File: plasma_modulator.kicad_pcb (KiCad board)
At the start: 4 copper layers, 100 x 80 mm, 74 parts, among them P1 CONN_01X03, P2 CONN_01X03, P3 CONN_01X06, P4 CONN_01X04, P5 RCA_1, Q1 MOSFET_N, Q2 MOSFET_N, Q3 MOSFET_N, Q4 MOSFET_N, SW1 SW_PUSH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

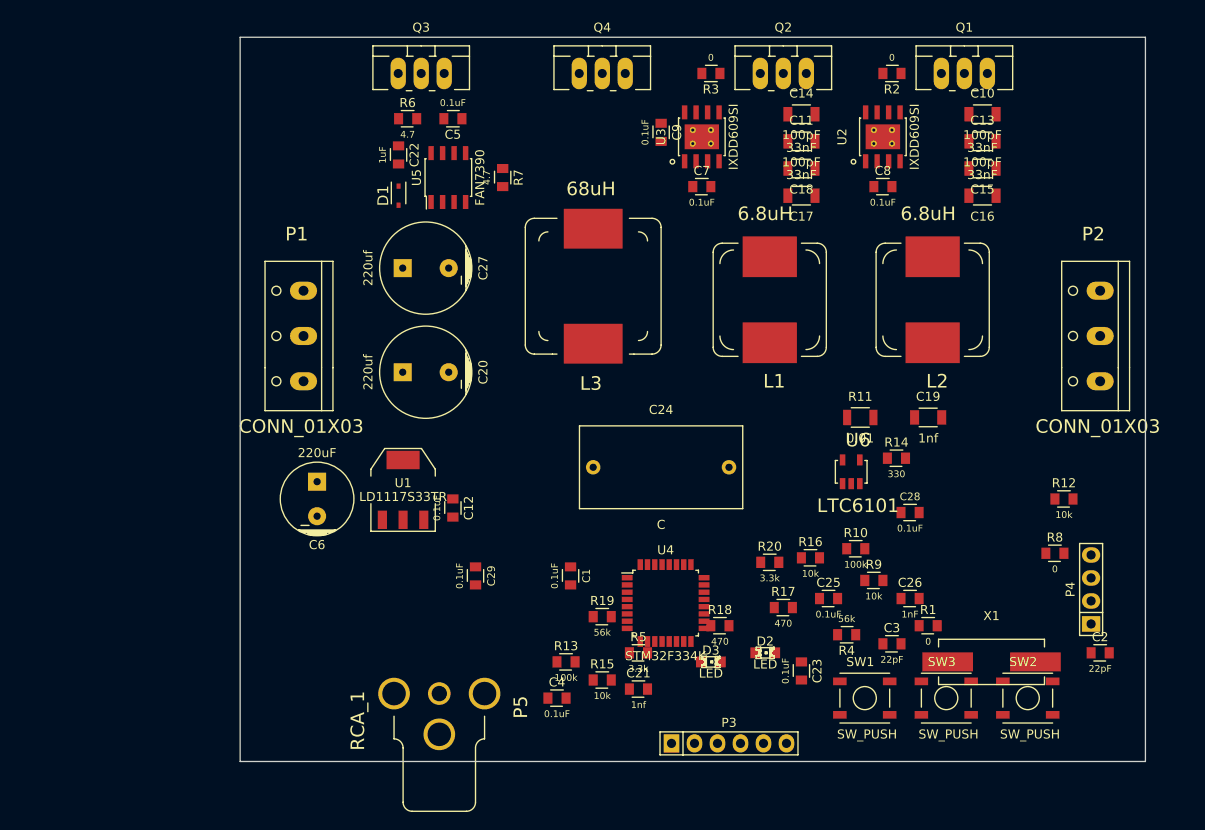
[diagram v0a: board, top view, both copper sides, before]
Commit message: draft of component layout
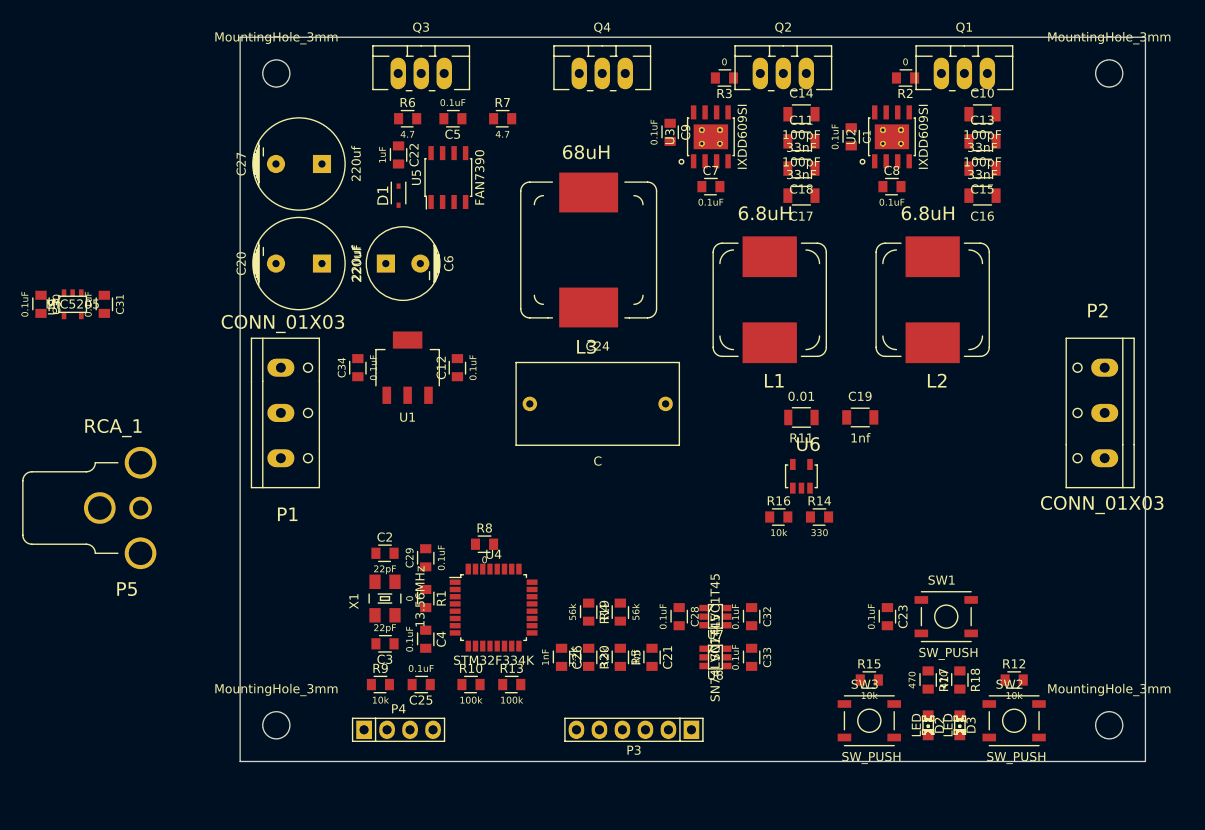
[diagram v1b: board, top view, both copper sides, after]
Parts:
- added C30: 0.1uF, wbraun_library:SMD-0805, F.Cu at (21.0, 80.5)
- added C31: 0.1uF, wbraun_library:SMD-0805, F.Cu at (28.0, 80.5)
- added C32: 0.1uF, wbraun_library:SMD-0805, F.Cu at (99.5, 115.0)
- added C33: 0.1uF, wbraun_library:SMD-0805, F.Cu at (99.5, 119.5)
- added C34: 0.1uF, wbraun_library:SMD-0805, F.Cu at (56.0, 87.5)
- added MountingHole_3mm: VAL**, Mounting_Holes:MountingHole_3mm, F.Cu at (47.0, 55.0)
- added MountingHole_3mm: VAL**, Mounting_Holes:MountingHole_3mm, F.Cu at (139.0, 55.0)
- added MountingHole_3mm: VAL**, Mounting_Holes:MountingHole_3mm, F.Cu at (47.0, 127.0)
- added MountingHole_3mm: VAL**, Mounting_Holes:MountingHole_3mm, F.Cu at (139.0, 127.0)
- added U7: SN74LVC1T45, SMD_Packages:SOT-23-6, F.Cu at (95.5, 115.0)
- added U8: SN74LVC1T45, SMD_Packages:SOT-23-6, F.Cu at (95.5, 119.5)
- added U9: MIC5205, SMD_Packages:SOT-23-5, F.Cu at (24.5, 80.5)
- U1: footprint SMD_Packages:SOT-223 -> wbraun_library:SOT-223
- X1: footprint Crystals:Crystal_HC49-SD_SMD -> wbraun_library:4-SMD
- moved C2 79.8 mm to (59.0, 108.0)
- moved P4 78.1 mm to (60.5, 127.5), turned to 0 degrees
- moved X1 67.4 mm to (59.0, 113.0), turned to 90 degrees
- moved R8 63.0 mm to (70.0, 107.0)
- moved C1 57.6 mm to (110.5, 62.0)
- moved C3 56.0 mm to (59.0, 118.0), turned to 180 degrees
- moved R9 55.7 mm to (58.5, 122.5)
- moved R1 55.6 mm to (63.5, 113.0), turned to 270 degrees
- moved C25 46.0 mm to (63.0, 122.5), turned to 180 degrees
- moved R10 45.1 mm to (68.5, 122.5)
- moved P5 45.1 mm to (27.5, 103.0), turned to 0 degrees
- moved C26 39.0 mm to (78.5, 119.5), turned to 270 degrees
- moved R15 29.5 mm to (112.5, 122.0)
- moved D3 28.4 mm to (122.5, 127.0), turned to 270 degrees
- moved C28 28.0 mm to (91.5, 115.0), turned to 270 degrees
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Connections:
- R17 pad 1: +3.3V -> STATUS_2
- R18 pad 1: STATUS -> STATUS_1
- U4 pad 14: STATUS -> Net-(U4-Pad14)
- U4 pad 20: RF_A -> RF_A_lv
- U4 pad 21: RF_B -> RF_B_lv
- U4 pad 29: Net-(U4-Pad29) -> STATUS_1
- U4 pad 30: Net-(U4-Pad30) -> STATUS_2

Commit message: final component placement
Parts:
- removed R8: 0, wbraun_library:SMD-0805
- moved C30 41.1 mm to (57.5, 99.5)
- moved C31 41.1 mm to (64.5, 99.5)
- moved U9 41.1 mm to (61.0, 99.5)
- moved P5 20.1 mm to (45.5, 112.0)
- moved R16 8.28 mm to (95.0, 100.5), turned to 90 degrees
- moved R11 5.70 mm to (99.5, 94.5)
- moved U6 5.59 mm to (99.5, 100.5)
- moved R14 4.61 mm to (104.0, 100.5), turned to 270 degrees
- moved C23 3.61 mm to (112.5, 112.0)
- moved D2 3.61 mm to (117.0, 124.0)
- moved D3 3.61 mm to (120.5, 124.0)
- moved R12 3.61 mm to (126.5, 119.0)
- moved R15 3.61 mm to (110.5, 119.0)
- moved R17 3.61 mm to (117.0, 119.0)
- moved R18 3.61 mm to (120.5, 119.0)
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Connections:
- U4 pad 31: BOOT0 -> GND
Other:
- outline, holes or cut-outs redrawn

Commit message: PCB ready for fab
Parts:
- added C35: 3.9nF, wbraun_library:SMD-0805, F.Cu at (73.0, 121.5)
- added C36: 0.1uF, wbraun_library:SMD-0805, F.Cu at (91.5, 121.5)
- added R21: 4.7, wbraun_library:SMD-0805, F.Cu at (57.2, 68.5)
- added R8: 1k, wbraun_library:SMD-0805, F.Cu at (68.5, 121.5)
- moved C19 3.72 mm to (106.0, 91.8)
- moved R14 3.69 mm to (102.2, 97.2)
- moved R16 3.40 mm to (94.0, 97.2)
- moved U6 3.35 mm to (98.0, 97.5)
- moved R11 3.04 mm to (99.0, 91.5)
- moved C12 3.00 mm to (66.5, 87.0)
- moved C30 3.00 mm to (57.5, 96.5)
- moved C31 3.00 mm to (64.5, 96.5), turned to 90 degrees
- moved U1 3.00 mm to (61.0, 87.0)
- moved U9 3.00 mm to (61.0, 96.5)
- moved R10 2.00 mm to (68.5, 124.5)
- moved R13 2.00 mm to (73.0, 124.5)
- moved L2 1.50 mm to (121.0, 80.0)
- moved C25 1.12 mm to (63.5, 121.5)
- moved R9 1.12 mm to (59.0, 121.5)
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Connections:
- C25 pad 1: AUDIO_ADC -> Net-(C25-Pad1)
- D1 pad 1: +12V -> Net-(D1-Pad1)
- P2 pad 2: RF_OUT_B -> RF_OUT_A
- P2 pad 3: RF_OUT_A -> RF_OUT_B
- P3 pad 3: SPI_CLK -> SPI_SCK
- R10 pad 2: AUDIO_ADC -> Net-(C25-Pad1)
- R13 pad 1: AUDIO_ADC -> Net-(C25-Pad1)
- U4 pad 14: Net-(U4-Pad14) -> LCD_D/C
- U4 pad 15: BUTTON_A -> Net-(U4-Pad15)
- U4 pad 27: LCD_D/C -> BUTTON_A
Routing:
- net GND: track 0.00 -> 668.4 mm, vias 0 -> 139
- net +3.3V: track 0.00 -> 253.9 mm, vias 0 -> 21
- net +12V: track 0.00 -> 221.9 mm, vias 0 -> 3
- net +48V: track 0.00 -> 110.3 mm, vias 0 -> 2
- net MOD_A: track 0.00 -> 84.4 mm, vias 0 -> 2
- net MOD_B: track 0.00 -> 84.4 mm, vias 0 -> 2
- net VDD: track 0.00 -> 80.6 mm, vias 0 -> 2
- net BUTTON_A: track 0.00 -> 69.9 mm, vias 0 -> 2
- net RF_B: track 0.00 -> 67.3 mm, vias 0 -> 2
- net +5V: track 0.00 -> 66.4 mm, vias 0 -> 3
- net reset: track 0.00 -> 65.2 mm, vias 0 -> 4
- net RF_A: track 0.00 -> 60.7 mm, vias 0 -> 2
- net RF_OUT_A: track 0.00 -> 60.2 mm, vias 0 -> 4
- net STATUS_1: track 0.00 -> 57.2 mm, vias 0 -> 2
- net STATUS_2: track 0.00 -> 54.7 mm, vias 0 -> 2
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- added copper zone on B.Cu, net +3.3V
- added copper zone on F.Cu, net +3.3V
- added copper zone on B.Cu, net GND
- added copper zone on F.Cu, net GND
- added copper zone on In1.Cu, net GND
- added copper zone on In2.Cu, net GND
- added copper zone on F.Cu, net Net-(C10-Pad1)
- added copper zone on F.Cu, net Net-(C11-Pad1)
- added copper zone on F.Cu, net RF_OUT_B
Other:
- net class Default: clearance 0.254 -> 0.1524; trace_width 0.254 -> 0.1524; via_dia 0.889 -> 0.6858; via_drill 0.635 -> 0.3302
- rule trace_clearance: 0.254 -> 0.1524
- rule trace_min: 0.254 -> 0.1524
- rule via_min_drill: 0.508 -> 0.3302
- rule via_min_size: 0.889 -> 0.6858
- board text added: "12V"
- board text added: "48V"
- board text added: "<"
- board text added: ">"
- board text added: "GND"
- board text added: "PROG"
- board text added: "Plasma Tweeter V2.0 wbraun@mit.edu"
- board text added: "RF"
- board text added: "reset"

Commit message: pcb sent to fab
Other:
- board text added: "version: ee016a0b60718e3f1cba29521216f913cf73a603"
